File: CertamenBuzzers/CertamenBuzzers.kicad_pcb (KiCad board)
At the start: 2 copper layers, 100 x 84.2 mm, 53 parts, among them J1 USB_C_Receptacle_USB2.0_14P, J10 C4, J11 B4, J12 A4, J14 C1, J2 B1, J3 A1, J4 C2, J5 B2, J6 A2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

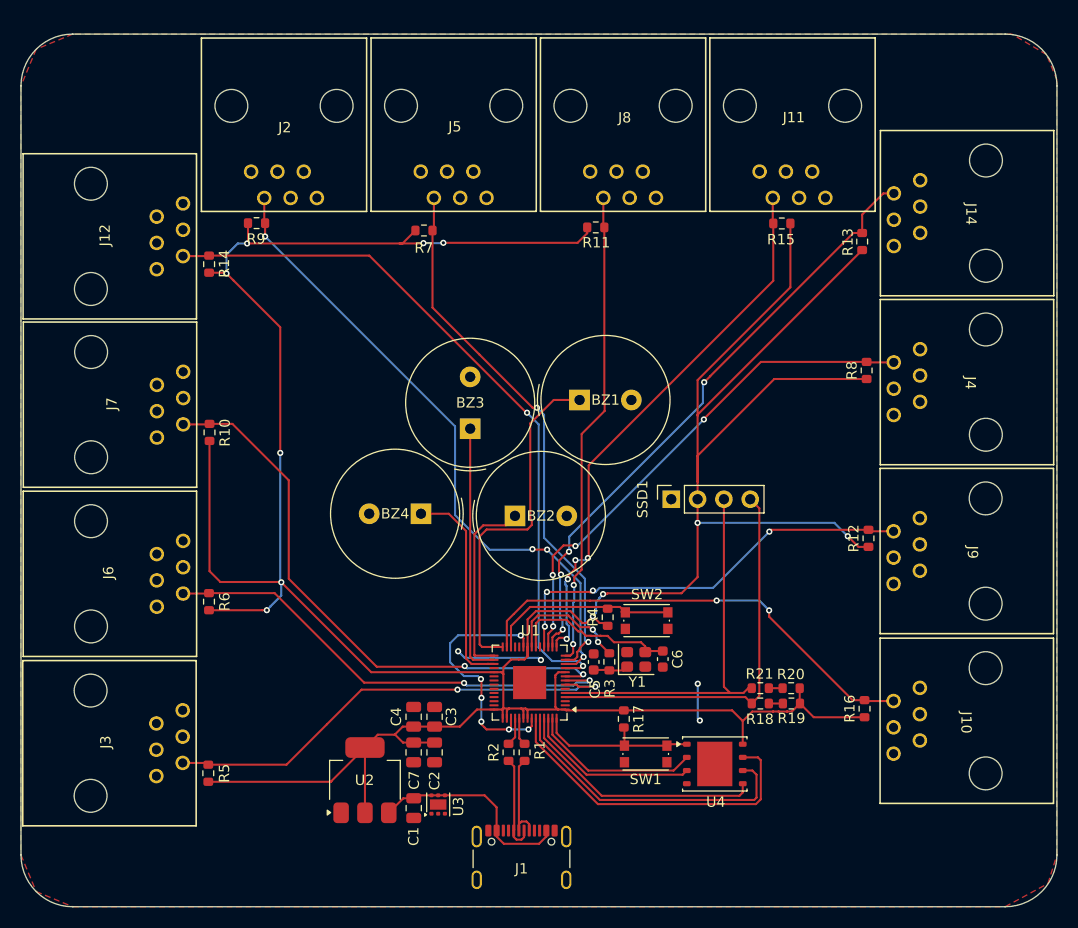
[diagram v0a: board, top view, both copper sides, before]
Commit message: pcb done + receptacles adjusted + 3d models added
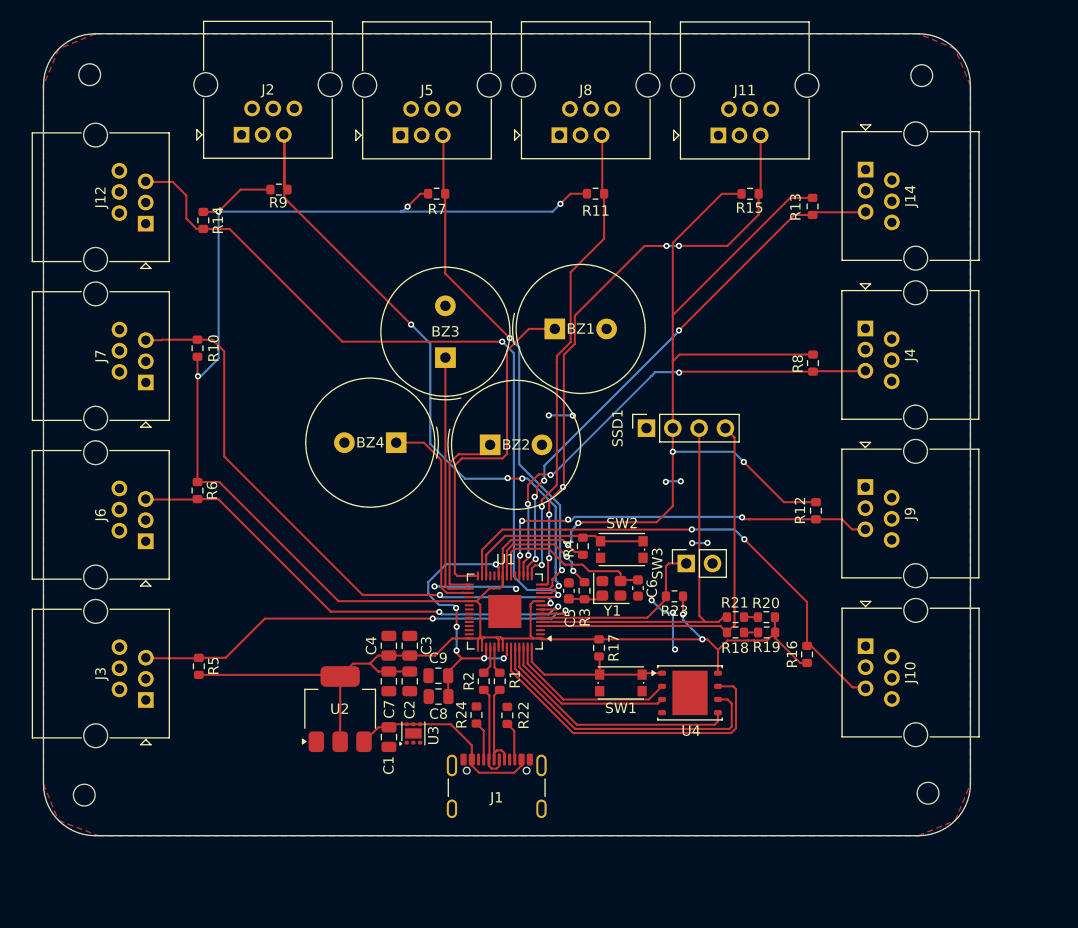
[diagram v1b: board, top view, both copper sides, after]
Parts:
- added C8: 10u, Capacitor_SMD:C_0805_2012Metric, F.Cu at (114.5, 134.6)
- added C9: 100n, Capacitor_SMD:C_0805_2012Metric, F.Cu at (114.4, 132.6)
- added R22: 10k, Resistor_SMD:R_0603_1608Metric, F.Cu at (121.1, 136.4)
- added R23: 10k, Resistor_SMD:R_0603_1608Metric, F.Cu at (137.2, 124.9)
- added R24: 10k, Resistor_SMD:R_0603_1608Metric, F.Cu at (118.1, 136.3)
- added REF**: MountingHole_2.1mm, MountingHole:MountingHole_2.1mm, F.Cu at (161.7, 143.9)
- added REF**: MountingHole_2.1mm, MountingHole:MountingHole_2.1mm, F.Cu at (80.8, 74.5)
- added REF**: MountingHole_2.1mm, MountingHole:MountingHole_2.1mm, F.Cu at (80.3, 144.1)
- added REF**: MountingHole_2.1mm, MountingHole:MountingHole_2.1mm, F.Cu at (161.1, 74.6)
- added SW3: SW_Push, Connector_PinSocket_2.54mm:PinSocket_1x02_P2.54mm_Vertical, F.Cu at (138.4, 121.7)
- J10, J11, J12, J14, J2, J3, J4, J5, J6, J7, J8, J9: footprint Buzzers:ADAMTECH_MTJ-88ARX1-FSM-LG -> Connector_RJ:RJ25_Wayconn_MJEA-660X1_Horizontal
- moved J11 12.0 mm to (141.5, 80.4)
- moved J8 11.1 mm to (126.1, 80.4)
- moved R6 10.8 mm to (91.2, 114.7), turned to -90 degrees
- moved J10 10.7 mm to (155.7, 129.7)
- moved R5 10.4 mm to (91.3, 131.6)
- moved J5 10.3 mm to (110.8, 80.4)
- moved J9 9.73 mm to (155.7, 114.3)
- moved J2 9.49 mm to (95.4, 80.3)
- moved J4 8.79 mm to (155.7, 99.0)
- moved R10 8.21 mm to (91.2, 100.9)
- moved J14 7.87 mm to (155.7, 83.7)
- moved R16 7.63 mm to (150.0, 130.5)
- moved R19 7.26 mm to (146.1, 128.4)
- moved C1 7.26 mm to (109.7, 138.5)
- moved C7 7.26 mm to (109.7, 133.1)
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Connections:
- J1 pad A5: GND -> Net-(J1-CC1)
- J1 pad B5: GND -> Net-(J1-CC2)
- U1 pad 14: /B3 -> /B4
- U1 pad 15: /B4 -> /B3
- U1 pad 6: unconnected-(U1-GPIO4-Pad6) -> Net-(U1-GPIO4)
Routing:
- net +3V3: track 352.7 -> 312.4 mm, vias 11 -> 10
- net Net-(U1-GPIO4): track 0.00 -> 18.1 mm
- net GND: track 12.0 -> 19.5 mm, vias 4 -> 11
- net /C1: track 59.2 -> 52.9 mm
- net /C4: track 45.0 -> 49.2 mm
- net /B4: track 53.7 -> 57.6 mm, vias 4 -> 5
- net Net-(J1-CC1): track 0.00 -> 3.77 mm
- net /C2: track 49.8 -> 46.2 mm
- net Net-(J1-CC2): track 0.00 -> 3.40 mm
- net +1V1: track 25.4 -> 28.7 mm
- net /B1: track 62.7 -> 65.8 mm
- net /A4: track 69.6 -> 72.2 mm
- net /B2: track 52.9 -> 50.3 mm
- net /C3: track 41.6 -> 39.4 mm
- net /A2: track 45.5 -> 46.7 mm
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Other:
- board size 100 x 84.2 mm -> 89.5 x 77.4 mm
